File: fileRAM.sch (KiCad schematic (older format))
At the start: 12 parts, among them J3 5530843-2, U35 74AHC273, U36 74AHC1G04, U37 74AHC273, U38 74AHC374, U39 74AHC1G04

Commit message: Apply MM1 memory standard, and shared power pin symbol fix
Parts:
- removed U36, U39: 74AHC1G04, Package_TO_SOT_SMD:SOT-23-5, symbol 74xGxx:74AHC1G04
- added U34: 74LVC1G34, Package_TO_SOT_SMD:SOT-23-5, symbol Custom:74LVC1G34
- added U36, U39: 74AHC1G04, Package_TO_SOT_SMD:SOT-23-5, symbol Custom:74AHC1G04
- J3: value 5530843-2 -> MM1_5530843-2
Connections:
- net labels added: B_RAM_~OE
- wire segments 86 -> 88
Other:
- note added: "MM1\nConnector 5530843-2 TE connectivity"
- note removed: "Connector 5530843-2 TE connectivity"
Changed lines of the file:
@@
 RAM_~CE
 Text Label 7550 1350 2    60   ~ 0
-RAM_~OE
+B_RAM_~OE
 Text Label 8050 1450 0    60   ~ 0
 RAM_~WE
@@
 	8150 1250 8050 1250
 Text Notes 8200 3000 0    60   ~ 0
-Connector 5530843-2 TE connectivity
+MM1\nConnector 5530843-2 TE connectivity
 Text HLabel 10300 850  2    60   Output ~ 0
 RAMDATA_[0..7]
@@
 Text Label 9450 4700 0    60   ~ 0
 RAMDATA_7
-Text Label 7650 5850 2    60   ~ 0
+Text Label 7600 5850 2    60   ~ 0
 RAM_~OE
-Text Label 4950 1900 0    60   ~ 0
+Text Label 4150 2850 0    60   ~ 0
 RAM_~WE
-$Comp
-L power:+5V #PWR096
-U 1 1 5B10C7DD
-P 2000 4550
-F 0 "#PWR096" H 2000 4400 50  0001 C CNN
-F 1 "+5V" H 2000 4690 50  0000 C CNN
-F 2 "" H 2000 4550 50  0000 C CNN
-F 3 "" H 2000 4550 50  0000 C CNN
-	1    2000 4550
-	1    0    0    -1
-$EndComp
 $Comp
 L power:GND #PWR097
@@
 Text Label 1500 5650 2    60   ~ 0
 NUMBER_7
-$Comp
-L power:+5V #PWR098
-U 1 1 5B10CD50
-P 4700 4550
-F 0 "#PWR098" H 4700 4400 50  0001 C CNN
-F 1 "+5V" H 4700 4690 50  0000 C CNN
-F 2 "" H 4700 4550 50  0000 C CNN
-F 3 "" H 4700 4550 50  0000 C CNN
-	1    4700 4550
-	1    0    0    -1
-$EndComp
 $Comp
 L power:GND #PWR099
@@
 	2000 6300 2000 6350
 $Comp
-L power:+5V #PWR?
-U 1 1 5CAAD011
-P 4700 1700
-AR Path="/5CAAD011" Ref="#PWR?"  Part="1"
-AR Path="/5B0E1E98/5CAAD011" Ref="#PWR0117"  Part="1"
-F 0 "#PWR0117" H 4700 1550 50  0001 C CNN
-F 1 "+5V" H 4700 1850 50  0000 C CNN
-F 2 "" H 4700 1700 50  0001 C CNN
-F 3 "" H 4700 1700 50  0001 C CNN
-	1    4700 1700
-	1    0    0    -1
-$EndComp
-$Comp
 L power:GND #PWR?
 U 1 1 5CAAD017
-P 4700 2100
+P 3850 3150
 AR Path="/5CAAD017" Ref="#PWR?"  Part="1"
 AR Path="/5B0E1E98/5CAAD017" Ref="#PWR0118"  Part="1"
-F 0 "#PWR0118" H 4700 1850 50  0001 C CNN
-F 1 "GND" H 4700 1950 50  0000 C CNN
-F 2 "" H 4700 2100 50  0001 C CNN
-F 3 "" H 4700 2100 50  0001 C CNN
-	1    4700 2100
-	1    0    0    -1
-$EndComp
-$Comp
-L 74xGxx:74AHC1G04 U?
-U 1 1 5CAAD01D
-P 4700 1900
-AR Path="/5CAAD01D" Ref="U?"  Part="1"
-AR Path="/5B0E1E98/5CAAD01D" Ref="U36"  Part="1"
-F 0 "U36" H 4800 2150 50  0000 C CNN
-F 1 "74AHC1G04" H 4950 2050 50  0000 C CNN
-F 2 "Package_TO_SOT_SMD:SOT-23-5" H 4700 1900 50  0001 C CNN
-F 3 "http://www.ti.com/lit/sg/scyt129e/scyt129e.pdf" H 4700 1900 50  0001 C CNN
-	1    4700 1900
-	1    0    0    -1
-$EndComp
-Wire Wire Line
-	4700 1700 4700 1800
-Wire Wire Line
-	4700 2000 4700 2100
+F 0 "#PWR0118" H 3850 2900 50  0001 C CNN
+F 1 "GND" H 3850 3000 50  0000 C CNN
+F 2 "" H 3850 3150 50  0001 C CNN
+F 3 "" H 3850 3150 50  0001 C CNN
+	1    3850 3150
+	1    0    0    -1
+$EndComp
+Wire Wire Line
+	3850 3050 3850 3150
 $Comp
 L Connector_Generic:Conn_02x15_Odd_Even J3
@@
 P 7750 1950
 F 0 "J3" H 7800 1025 50  0000 C CNN
-F 1 "5530843-2" H 7800 1116 50  0000 C CNN
+F 1 "MM1_5530843-2" H 7800 1116 50  0000 C CNN
 F 2 "TE5530843-2:TE_5530843-2" H 7750 1950 50  0001 C CNN
 F 3 "~" H 7750 1950 50  0001 C CNN
@@
 L power:+5V #PWR?
 U 1 1 5CB02F69
-P 7950 5650
+P 7900 5550
 AR Path="/5CB02F69" Ref="#PWR?"  Part="1"
 AR Path="/5B0E1E98/5CB02F69" Ref="#PWR0119"  Part="1"
-F 0 "#PWR0119" H 7950 5500 50  0001 C CNN
-F 1 "+5V" H 7950 5800 50  0000 C CNN
-F 2 "" H 7950 5650 50  0001 C CNN
-F 3 "" H 7950 5650 50  0001 C CNN
-	1    7950 5650
+F 0 "#PWR0119" H 7900 5400 50  0001 C CNN
+F 1 "+5V" H 7900 5700 50  0000 C CNN
+F 2 "" H 7900 5550 50  0001 C CNN
+F 3 "" H 7900 5550 50  0001 C CNN
+	1    7900 5550
 	1    0    0    -1
 $EndComp
@@
 L power:GND #PWR?
 U 1 1 5CB02F6F
-P 7950 6050
+P 7900 6150
 AR Path="/5CB02F6F" Ref="#PWR?"  Part="1"
 AR Path="/5B0E1E98/5CB02F6F" Ref="#PWR0120"  Part="1"
-F 0 "#PWR0120" H 7950 5800 50  0001 C CNN
-F 1 "GND" H 7950 5900 50  0000 C CNN
-F 2 "" H 7950 6050 50  0001 C CNN
-F 3 "" H 7950 6050 50  0001 C CNN
-	1    7950 6050
-	1    0    0    -1
-$EndComp
-$Comp
-L 74xGxx:74AHC1G04 U?
-U 1 1 5CB02F75
-P 7950 5850
-AR Path="/5CB02F75" Ref="U?"  Part="1"
-AR Path="/5B0E1E98/5CB02F75" Ref="U39"  Part="1"
-F 0 "U39" H 8100 6100 50  0000 C CNN
-F 1 "74AHC1G04" H 8200 6000 50  0000 C CNN
-F 2 "Package_TO_SOT_SMD:SOT-23-5" H 7950 5850 50  0001 C CNN
-F 3 "http://www.ti.com/lit/sg/scyt129e/scyt129e.pdf" H 7950 5850 50  0001 C CNN
-	1    7950 5850
-	1    0    0    -1
-$EndComp
-Wire Wire Line
-	7950 5650 7950 5750
-Wire Wire Line
-	7950 5950 7950 6050
+F 0 "#PWR0120" H 7900 5900 50  0001 C CNN
+F 1 "GND" H 7900 6000 50  0000 C CNN
+F 2 "" H 7900 6150 50  0001 C CNN
+F 3 "" H 7900 6150 50  0001 C CNN
+	1    7900 6150
+	1    0    0    -1
+$EndComp
+Wire Wire Line
+	7900 5550 7900 5650
+Wire Wire Line
+	7900 6050 7900 6150
 $Comp
 L Device:C C37
@@
 F 3 "https://assets.nexperia.com/documents/data-sheet/74AHC_AHCT374.pdf" H 8950 4500 50  0001 C CNN
 	1    8950 4500
-	1    0    0    -1
-$EndComp
-$Comp
-L power:+5V #PWR088
-U 1 1 5B103994
-P 8950 3600
-F 0 "#PWR088" H 8950 3450 50  0001 C CNN
-F 1 "+5V" H 8950 3740 50  0000 C CNN
-F 2 "" H 8950 3600 50  0000 C CNN
-F 3 "" H 8950 3600 50  0000 C CNN
-	1    8950 3600
 	1    0    0    -1
 $EndComp
@@
 Text Label 8450 4900 2    60   ~ 0
 BRAMDATA_CLK
-Text Label 4400 1900 2    60   ~ 0
+Text Label 3550 2850 2    60   ~ 0
 RAMWRITE_CLK
 Text Label 1500 5850 2    60   ~ 0
@@
 Text Label 4200 5850 2    60   ~ 0
 BRAMADD2_CLK
+$Comp
+L power:+3.3V #PWR0154
+U 1 1 5F37ECCC
+P 2000 4550
+F 0 "#PWR0154" H 2000 4400 50  0001 C CNN
+F 1 "+3.3V" H 2015 4723 50  0000 C CNN
+F 2 "" H 2000 4550 50  0001 C CNN
+F 3 "" H 2000 4550 50  0001 C CNN
+	1    2000 4550
+	1    0    0    -1
+$EndComp
+$Comp
+L power:+3.3V #PWR0155
+U 1 1 5F38224D
+P 4700 4550
+F 0 "#PWR0155" H 4700 4400 50  0001 C CNN
+F 1 "+3.3V" H 4715 4723 50  0000 C CNN
+F 2 "" H 4700 4550 50  0001 C CNN
+F 3 "" H 4700 4550 50  0001 C CNN
+	1    4700 4550
+	1    0    0    -1
+$EndComp
+$Comp
+L power:+3.3V #PWR0156
+U 1 1 5F384E0F
+P 8950 3600
+F 0 "#PWR0156" H 8950 3450 50  0001 C CNN
+F 1 "+3.3V" H 8965 3773 50  0000 C CNN
+F 2 "" H 8950 3600 50  0001 C CNN
+F 3 "" H 8950 3600 50  0001 C CNN
+	1    8950 3600
+	1    0    0    -1
+$EndComp
+$Comp
+L power:+3.3V #PWR0117
+U 1 1 5F385A0B
+P 3850 2550
+F 0 "#PWR0117" H 3850 2400 50  0001 C CNN
+F 1 "+3.3V" H 3865 2723 50  0000 C CNN
+F 2 "" H 3850 2550 50  0001 C CNN
+F 3 "" H 3850 2550 50  0001 C CNN
+	1    3850 2550
+	1    0    0    -1
+$EndComp
+$Comp
+L Custom:74AHC1G04 U36
+U 1 1 5F3BE90E
+P 3850 2850
+F 0 "U36" H 4000 3100 50  0000 L CNN
+F 1 "74AHC1G04" H 4000 3000 50  0000 L CNN
+F 2 "Package_TO_SOT_SMD:SOT-23-5" H 3850 2850 50  0001 C CNN
+F 3 "https://assets.nexperia.com/documents/data-sheet/74AHC_AHCT1G04.pdf" H 3850 2850 50  0001 C CNN
+	1    3850 2850
+	1    0    0    -1
+$EndComp
+$Comp
+L Custom:74AHC1G04 U39
+U 1 1 5F3D1A99
+P 7900 5850
+F 0 "U39" H 8000 6100 50  0000 L CNN
+F 1 "74AHC1G04" H 8000 6000 50  0000 L CNN
+F 2 "Package_TO_SOT_SMD:SOT-23-5" H 7900 5850 50  0001 C CNN
+F 3 "https://assets.nexperia.com/documents/data-sheet/74AHC_AHCT1G04.pdf" H 7900 5850 50  0001 C CNN
+	1    7900 5850
+	1    0    0    -1
+$EndComp
+$Comp
+L Custom:74LVC1G34 U34
+U 1 1 5F4C25E9
+P 3850 1750
+F 0 "U34" H 4000 2050 50  0000 L CNN
+F 1 "74LVC1G34" H 4000 1950 50  0000 L CNN
+F 2 "Package_TO_SOT_SMD:SOT-23-5" H 3850 1750 50  0001 C CNN
+F 3 "https://assets.nexperia.com/documents/data-sheet/74LVC1G34.pdf" H 3850 1750 50  0001 C CNN
+	1    3850 1750
+	1    0    0    -1
+$EndComp
+Wire Wire Line
+	3850 2650 3850 2550
+$Comp
+L power:+3.3V #PWR0157
+U 1 1 5F4C305B
+P 3850 1450
+F 0 "#PWR0157" H 3850 1300 50  0001 C CNN
+F 1 "+3.3V" H 3865 1623 50  0000 C CNN
+F 2 "" H 3850 1450 50  0001 C CNN
+F 3 "" H 3850 1450 50  0001 C CNN
+	1    3850 1450
+	1    0    0    -1
+$EndComp
+Wire Wire Line
+	3850 1550 3850 1450
+$Comp
+L power:GND #PWR?
+U 1 1 5F4C5561
+P 3850 2050
+AR Path="/5F4C5561" Ref="#PWR?"  Part="1"
+AR Path="/5B0E1E98/5F4C5561" Ref="#PWR0158"  Part="1"
+F 0 "#PWR0158" H 3850 1800 50  0001 C CNN
+F 1 "GND" H 3850 1900 50  0000 C CNN
+F 2 "" H 3850 2050 50  0001 C CNN
+F 3 "" H 3850 2050 50  0001 C CNN
+	1    3850 2050
+	1    0    0    -1
+$EndComp
+Wire Wire Line
+	3850 1950 3850 2050
+Text Label 4150 1750 0    60   ~ 0
+B_RAM_~OE
+Text Label 3550 1750 2    60   ~ 0
+RAM_~OE
 Wire Bus Line
 	1550 3200 1550 4000

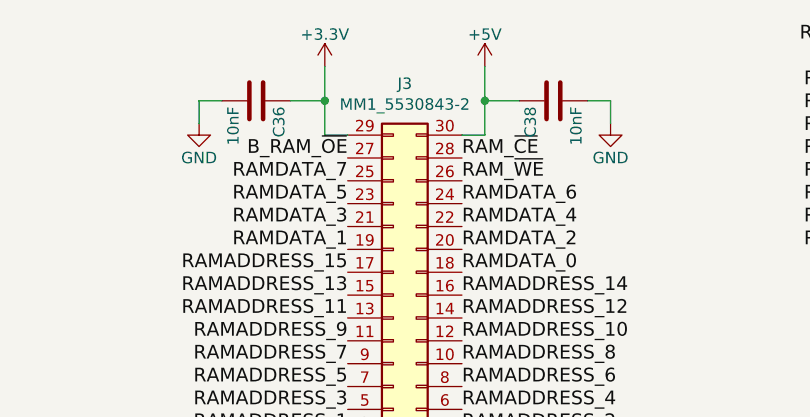
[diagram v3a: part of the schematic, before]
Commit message: V5.1 (#9)
* Apply new symbol for XC2C256-VQ100 #5

* Set new date and 5.1

* Replacing 74HC165 with 74HC166, and add SPI_CFG_DS #4

* Replace some gates with a 74AHC1G02 to fix the pulse problem #3

* Go next only if SRCVALUE, (simple instruction)

* Remove weird ghost bus in register

* Small cleaning in fileRegister

* Go next only if SRCVALUE, (complex instruction) #8
adding 74AHC1G08

* Better decoupling #6

* Component association (#7)

* netlist

* Updated BOM for V5.1

* Routing, cleaning first pass

* bit of pcb cleaning

* SolderMaskClearance to 0

* Schematics to pdf

* PCB files in pdf

* exporting Gerbert files

* new 3d images

* Update README.md

* Modifying CHANGELOG file

* Update README.md
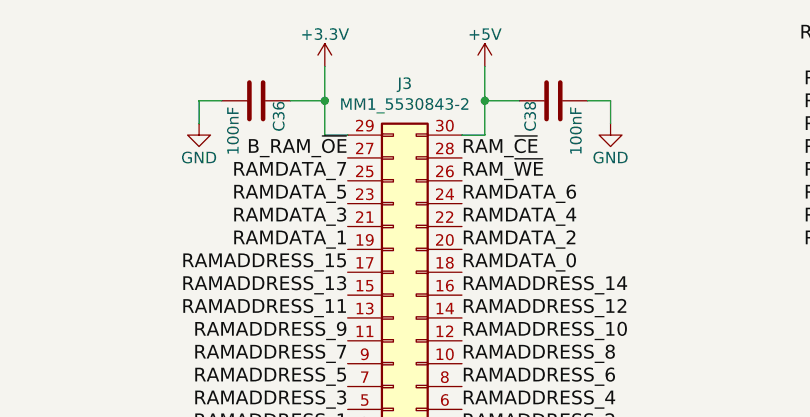
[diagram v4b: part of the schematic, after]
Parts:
- C36, C38: value 10nF -> 100nF
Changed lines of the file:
@@
 Sheet 5 8
 Title "GP8B"
-Date "2020-08-19"
-Rev "V5.0"
+Date "2021-03-04"
+Rev "V5.1"
 Comp "Guillaume Guillet"
-Comment1 "Copyright Guillaume Guillet 2020"
+Comment1 "Copyright Guillaume Guillet 2021"
 Comment2 "Licensed under CERN-OHL-W v2 or later"
 Comment3 ""
@@
 U 1 1 5B0E7716
 P 7150 1100
-F 0 "C36" H 7175 1200 50  0000 L CNN
-F 1 "10nF" H 7175 1000 50  0000 L CNN
+F 0 "C36" H 7150 1200 50  0000 L CNN
+F 1 "100nF" H 7175 1000 50  0000 L CNN
 F 2 "Capacitor_SMD:C_0805_2012Metric" H 7188 950 50  0001 C CNN
 F 3 "" H 7150 1100 50  0001 C CNN
@@
 U 1 1 5B0E7789
 P 8450 1100
-F 0 "C38" H 8475 1200 50  0000 L CNN
-F 1 "10nF" H 8475 1000 50  0000 L CNN
+F 0 "C38" H 8450 1200 50  0000 L CNN
+F 1 "100nF" H 8475 1000 50  0000 L CNN
 F 2 "Capacitor_SMD:C_0805_2012Metric" H 8488 950 50  0001 C CNN
 F 3 "" H 8450 1100 50  0001 C CNN
